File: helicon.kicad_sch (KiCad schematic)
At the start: 9 parts, among them J1 USB_C_Receptacle_USB2.0_16P, U1 STM32F411CEUx, U2 NCP1117-3.3_SOT223

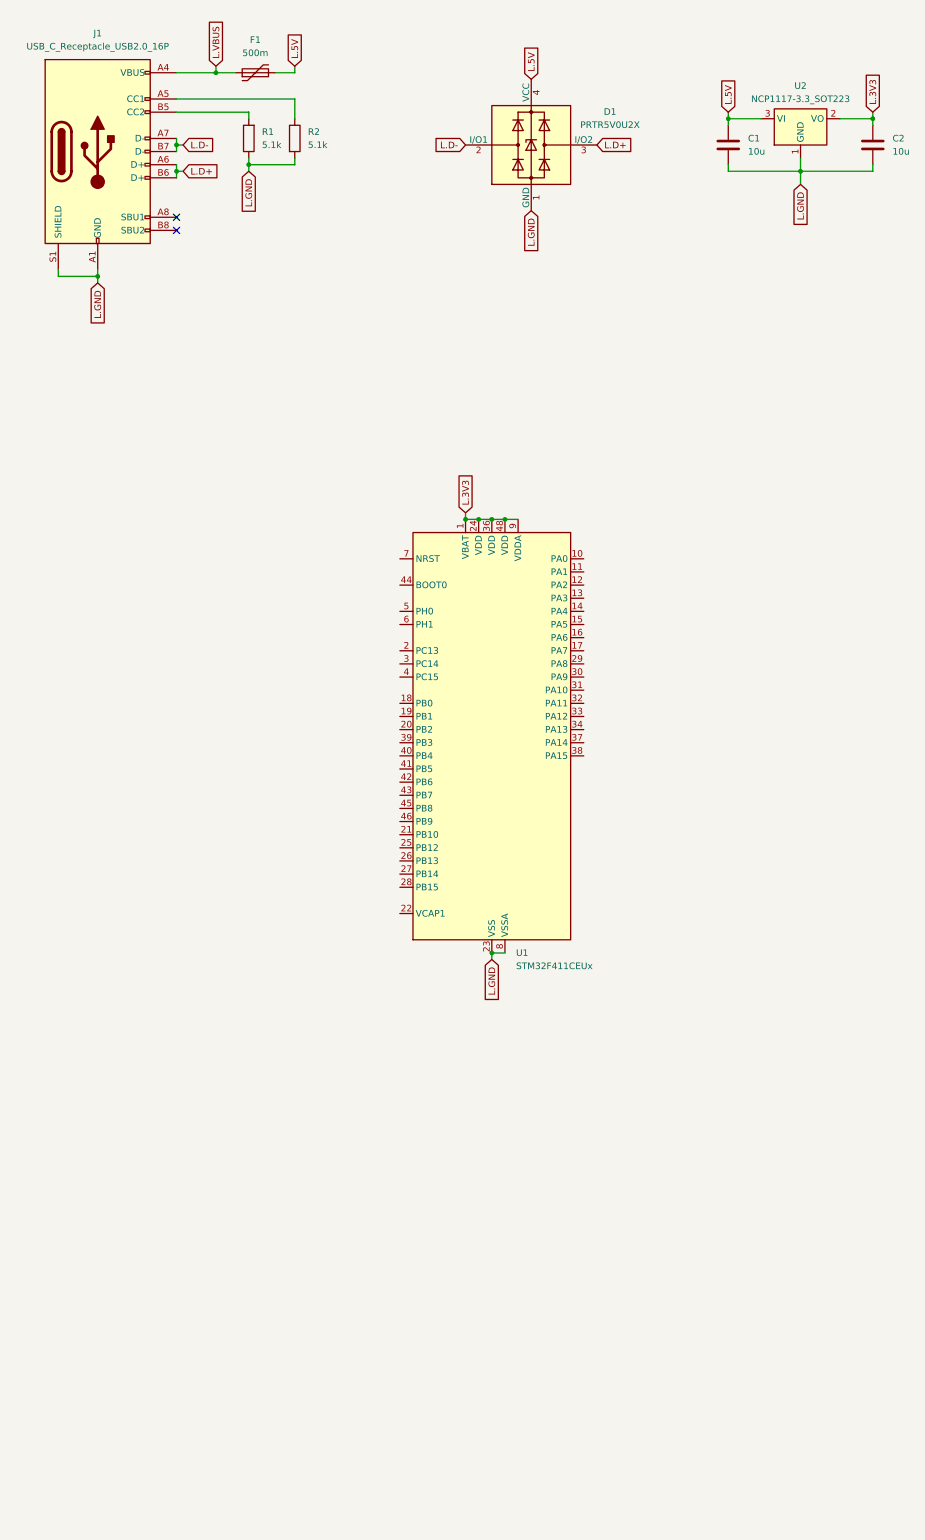
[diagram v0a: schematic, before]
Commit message: mcu schematic finished
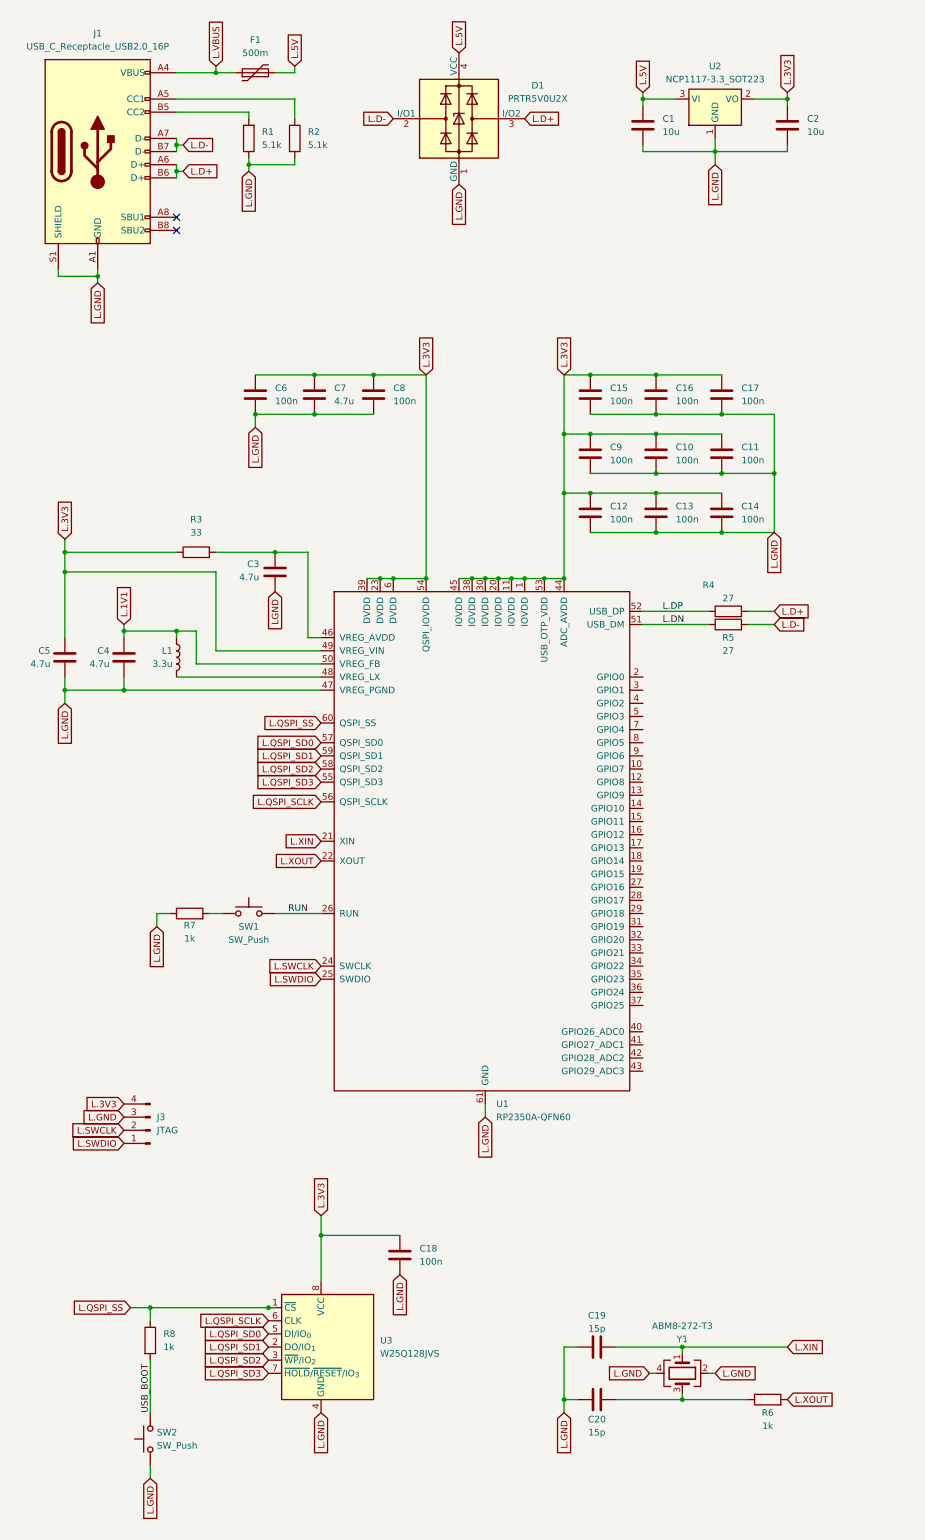
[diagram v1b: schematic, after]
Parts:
- removed U1: STM32F411CEUx, Package_DFN_QFN:QFN-48-1EP_7x7mm_P0.5mm_EP5.6x5.6mm, symbol MCU_ST_STM32F4:STM32F411CEUx
- added C10, C11, C12, C13, C14, C15, C16, C17, C18, C6, C8, C9: 100n, symbol Device:C
- added C19, C20: 15p, symbol Device:C
- added C3, C4, C5, C7: 4.7u, symbol Device:C
- added J3: JTAG, symbol Connector:Conn_01x04_Pin
- added L1: 3.3u, symbol Device:L
- added R3: 33, symbol Device:R
- added R4, R5: 27, symbol Device:R
- added R6, R7, R8: 1k, symbol Device:R
- added SW1, SW2: SW_Push, symbol Switch:SW_Push
- added U1: RP2350A-QFN60, symbol Custom:RP2350A-QFN60
- added U3: W25Q128JVS, Package_SO:SOIC-8_5.3x5.3mm_P1.27mm, symbol Memory_Flash:W25Q128JVS
- added Y1: ABM8-272-T3, symbol Device:Crystal_GND24
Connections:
- net L.3V3: now also C10.1, C11.1, C12.1, C13.1, C14.1, C15.1, C16.1, C17.1, C18.1, C5.1, C6.1, C7.1, C8.1, C9.1, J3.4 (Pin_4), R3.1, U1.1 (IOVDD), U1.11 (IOVDD), U1.20 (IOVDD), U1.23 (DVDD), U1.30 (IOVDD), U1.38 (IOVDD), U1.39 (DVDD), U1.44 (ADC_AVDD), U1.45 (IOVDD), U1.49 (VREG_VIN), U1.53 (USB_OTP_VDD), U1.54 (QSPI_IOVDD), U1.6 (DVDD), U3.8 (VCC)
- net L.D+: now also R4.2
- net L.D-: now also R5.2
- net L.GND: now also C10.2, C11.2, C12.2, C13.2, C14.2, C15.2, C16.2, C17.2, C18.2, C19.1, C20.1, C4.2, C5.2, C6.2, C7.2, C8.2, C9.2, J3.3 (Pin_3), R7.1, SW2.1, U1.47 (VREG_PGND), U1.61 (GND), U3.4 (GND), Y1.2, Y1.4
- new net: C3.1, R3.2, U1.46 (VREG_AVDD)
- new net: C20.2, R6.1, Y1.3
- new net: L1.2, U1.48 (VREG_LX)
- new net: R7.2, SW1.1
- new net L.1V1: C4.1, L1.1, U1.50 (VREG_FB)
- new net L.DN: R5.1, U1.51 (USB_DM)
- new net L.DP: R4.1, U1.52 (USB_DP)
- new net L.QSPI_SCLK: U1.56 (QSPI_SCLK), U3.6 (CLK)
- new net L.QSPI_SD0: U1.57 (QSPI_SD0), U3.5 (DI/IO_{0})
- new net L.QSPI_SD1: U1.59 (QSPI_SD1), U3.2 (DO/IO_{1})
- new net L.QSPI_SD2: U1.58 (QSPI_SD2), U3.3 (~{WP}/IO_{2})
- new net L.QSPI_SD3: U1.55 (QSPI_SD3), U3.7 (~{HOLD}/~{RESET}/IO_{3})
- new net L.QSPI_SS: R8.1, U1.60 (QSPI_SS), U3.1 (~{CS})
- new net L.SWCLK: J3.2 (Pin_2), U1.24 (SWCLK)
- new net L.SWDIO: J3.1 (Pin_1), U1.25 (SWDIO)
- new net L.XIN: C19.2, U1.21 (XIN), Y1.1
- new net L.XOUT: R6.2, U1.22 (XOUT)
- new net LGND: C3.2
- new net RUN: SW1.2, U1.26 (RUN)
- new net USB_BOOT: R8.2, SW2.2
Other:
- moved on the sheet: C1, C2, D1, U2
